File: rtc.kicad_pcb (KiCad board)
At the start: 2 copper layers, 50 x 30 mm, 8 parts, among them J1 Conn_01x05, U1 DS1302N+, Y1 32.768kHz

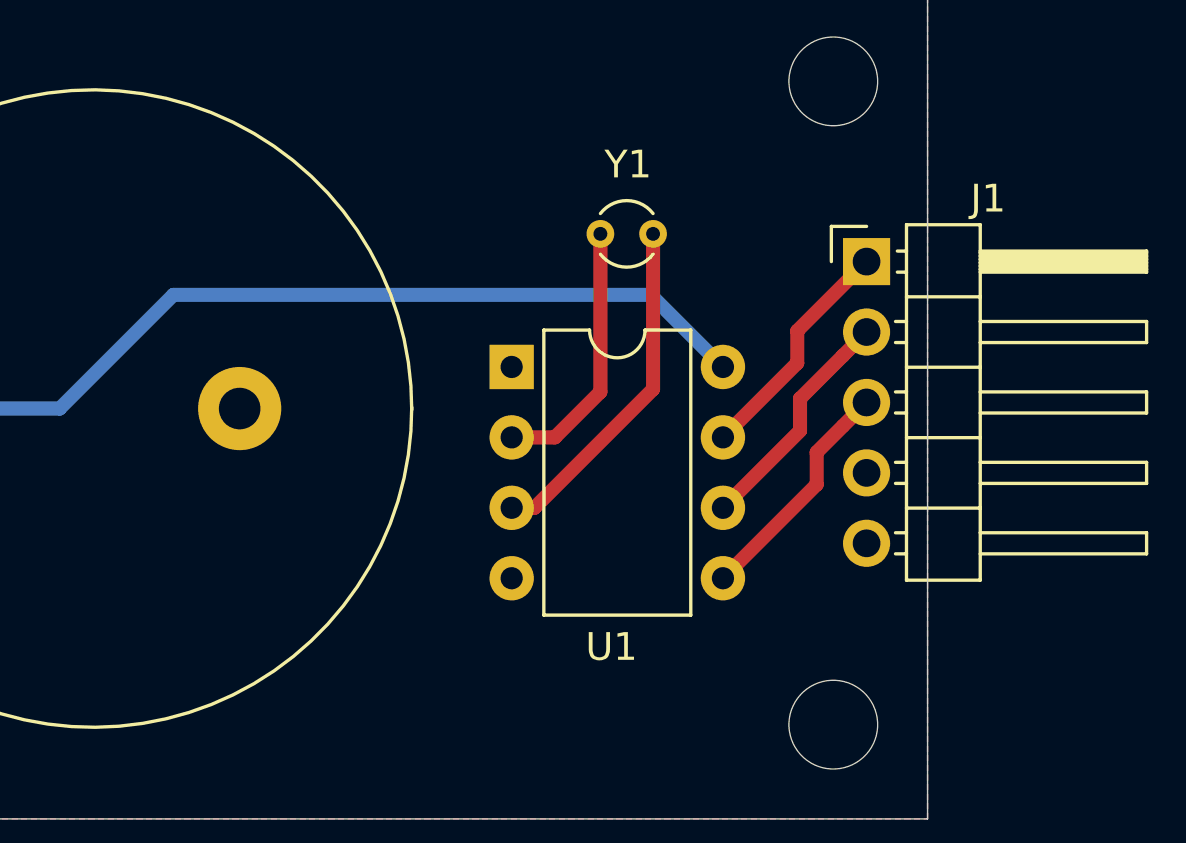
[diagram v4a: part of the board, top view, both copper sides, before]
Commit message: Clean up silk screen labels
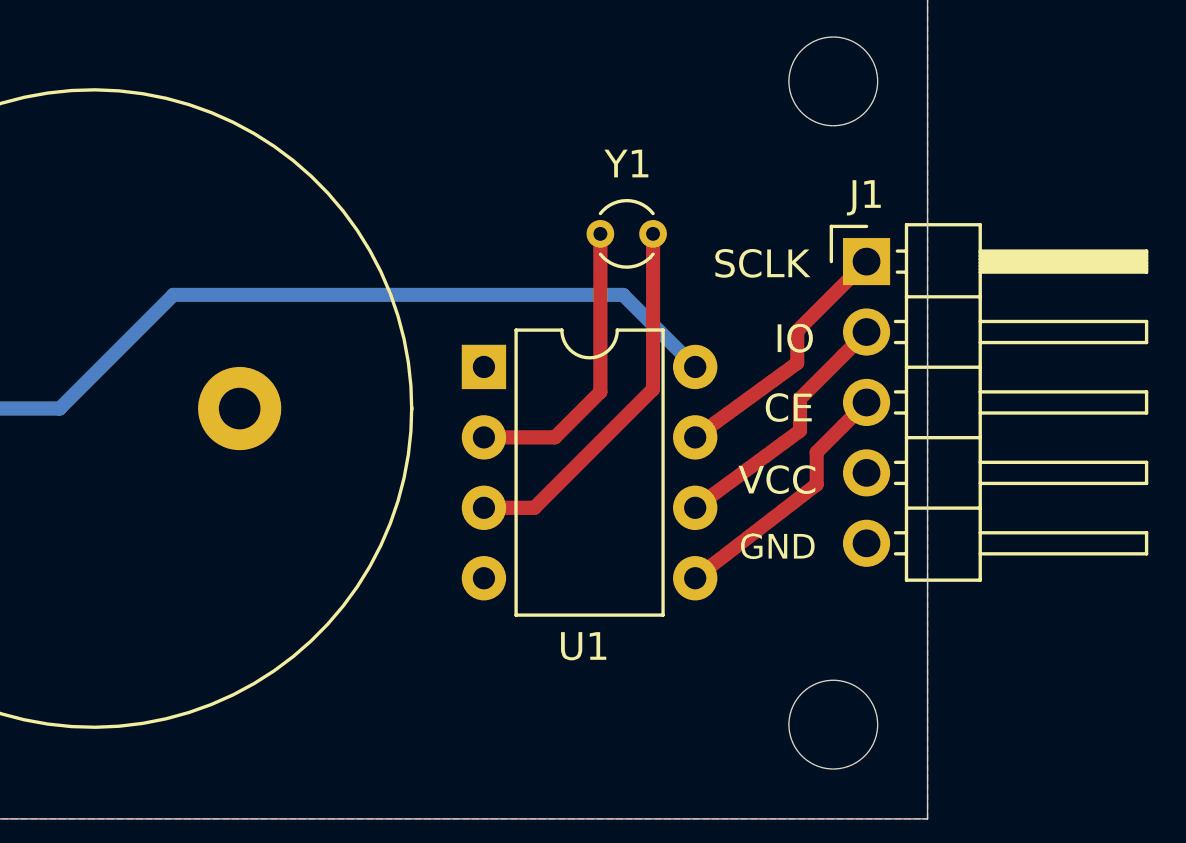
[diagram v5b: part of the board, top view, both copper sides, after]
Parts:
- moved U1 1.00 mm to (60.0, 44.7)
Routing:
- net Net-(U1-Pad3): track 12.5 -> 13.5 mm
- net Net-(U1-Pad2): track 9.58 -> 10.6 mm
- net Net-(BT1-Pad1): track 40.7 -> 39.7 mm
- net /SCLK: track 8.49 -> 9.25 mm
- net /IO: track 8.49 -> 9.25 mm
- net /CE: track 8.49 -> 9.24 mm
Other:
- board text added: "CE"
- board text added: "GND"
- board text added: "IO"
- board text added: "SCLK"
- board text added: "VCC"
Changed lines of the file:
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@@
   (general
     (thickness 1.6)
-    (drawings 15)
+    (drawings 20)
     (tracks 22)
     (zones 0)
@@
   )
   (module Package_DIP:DIP-8_W7.62mm (layer F.Cu)
-    (at 61 44.7)
+    (at 60 44.7)
     (descr "8-lead though-hole mounted DIP package, row spacing 7.62 mm (300 mils)")
     (tags "THT DIP DIL PDIP 2.54mm 7.62mm 300mil")
@@
     (descr "Through hole angled pin header, 1x05, 2.54mm pitch, 6mm pin length, single row")
     (tags "Through hole angled pin header THT 1x05 2.54mm single row")
-    (fp_text reference J1 (at 4.385 -2.27) (layer F.SilkS)
+    (fp_text reference J1 (at 0 -2.4) (layer F.SilkS)
       (effects (font (size 1 1) (thickness 0.15)))
     )
@@
     )
   )
+  (gr_text SCLK (at 70 41) (layer F.SilkS)
+    (effects (font (size 1 1) (thickness 0.15)))
+  )
+  (gr_text IO (at 71.2 43.7) (layer F.SilkS)
+    (effects (font (size 1 1) (thickness 0.15)))
+  )
+  (gr_text CE (at 71 46.2) (layer F.SilkS)
+    (effects (font (size 1 1) (thickness 0.15)))
+  )
+  (gr_text VCC (at 70.6 48.8) (layer F.SilkS)
+    (effects (font (size 1 1) (thickness 0.15)))
+  )
+  (gr_text GND (at 70.6 51.2) (layer F.SilkS)
+    (effects (font (size 0.889 0.889) (thickness 0.15)))
+  )
   (dimension 3.4 (width 0.12) (layer Dwgs.User)
     (gr_text "3.400 mm" (at 78.47 32.7 90) (layer Dwgs.User)
@@
   )
   (via (at 32.1 46) (size 0.762) (drill 0.4318) (layers F.Cu B.Cu) (net 2))
-  (segment (start 66.02 42.1) (end 68.62 44.7) (width 0.508) (layer B.Cu) (net 2))
-  (segment (start 48.8 42.1) (end 66.02 42.1) (width 0.508) (layer B.Cu) (net 2))
   (segment (start 30.7 46.2) (end 44.7 46.2) (width 0.508) (layer B.Cu) (net 2))
   (segment (start 44.7 46.2) (end 48.8 42.1) (width 0.508) (layer B.Cu) (net 2))
+  (segment (start 65.02 42.1) (end 67.62 44.7) (width 0.508) (layer B.Cu) (net 2))
+  (segment (start 48.8 42.1) (end 65.02 42.1) (width 0.508) (layer B.Cu) (net 2))
   (segment (start 71.3 43.4) (end 73.8 40.9) (width 0.508) (layer F.Cu) (net 4))
-  (segment (start 68.62 47.24) (end 71.3 44.56) (width 0.508) (layer F.Cu) (net 4))
+  (segment (start 67.62 47.24) (end 71.3 44.56) (width 0.508) (layer F.Cu) (net 4))
   (segment (start 71.3 44.56) (end 71.3 43.4) (width 0.508) (layer F.Cu) (net 4))
   (segment (start 72.950001 44.289999) (end 73.8 43.44) (width 0.508) (layer F.Cu) (net 5))
   (segment (start 71.4 45.84) (end 72.950001 44.289999) (width 0.508) (layer F.Cu) (net 5))
-  (segment (start 68.62 49.78) (end 71.4 47) (width 0.508) (layer F.Cu) (net 5))
+  (segment (start 67.62 49.78) (end 71.4 47) (width 0.508) (layer F.Cu) (net 5))
   (segment (start 71.4 47) (end 71.4 45.84) (width 0.508) (layer F.Cu) (net 5))
   (segment (start 72.950001 46.829999) (end 73.8 45.98) (width 0.508) (layer F.Cu) (net 6))
   (segment (start 72 47.78) (end 72.950001 46.829999) (width 0.508) (layer F.Cu) (net 6))
-  (segment (start 68.62 52.32) (end 72 48.94) (width 0.508) (layer F.Cu) (net 6))
+  (segment (start 67.62 52.32) (end 72 48.94) (width 0.508) (layer F.Cu) (net 6))
   (segment (start 72 48.94) (end 72 47.78) (width 0.508) (layer F.Cu) (net 6))
-  (segment (start 62.56 47.24) (end 61 47.24) (width 0.508) (layer F.Cu) (net 7))
+  (segment (start 62.56 47.24) (end 60 47.24) (width 0.508) (layer F.Cu) (net 7))
   (segment (start 64.2 39.9) (end 64.2 45.6) (width 0.508) (layer F.Cu) (net 7))
   (segment (start 64.2 45.6) (end 62.56 47.24) (width 0.508) (layer F.Cu) (net 7))
-  (segment (start 61.82 49.78) (end 61 49.78) (width 0.508) (layer F.Cu) (net 8))
+  (segment (start 61.82 49.78) (end 60 49.78) (width 0.508) (layer F.Cu) (net 8))
   (segment (start 66.1 39.9) (end 66.1 45.5) (width 0.508) (layer F.Cu) (net 8))
   (segment (start 66.1 45.5) (end 61.82 49.78) (width 0.508) (layer F.Cu) (net 8))

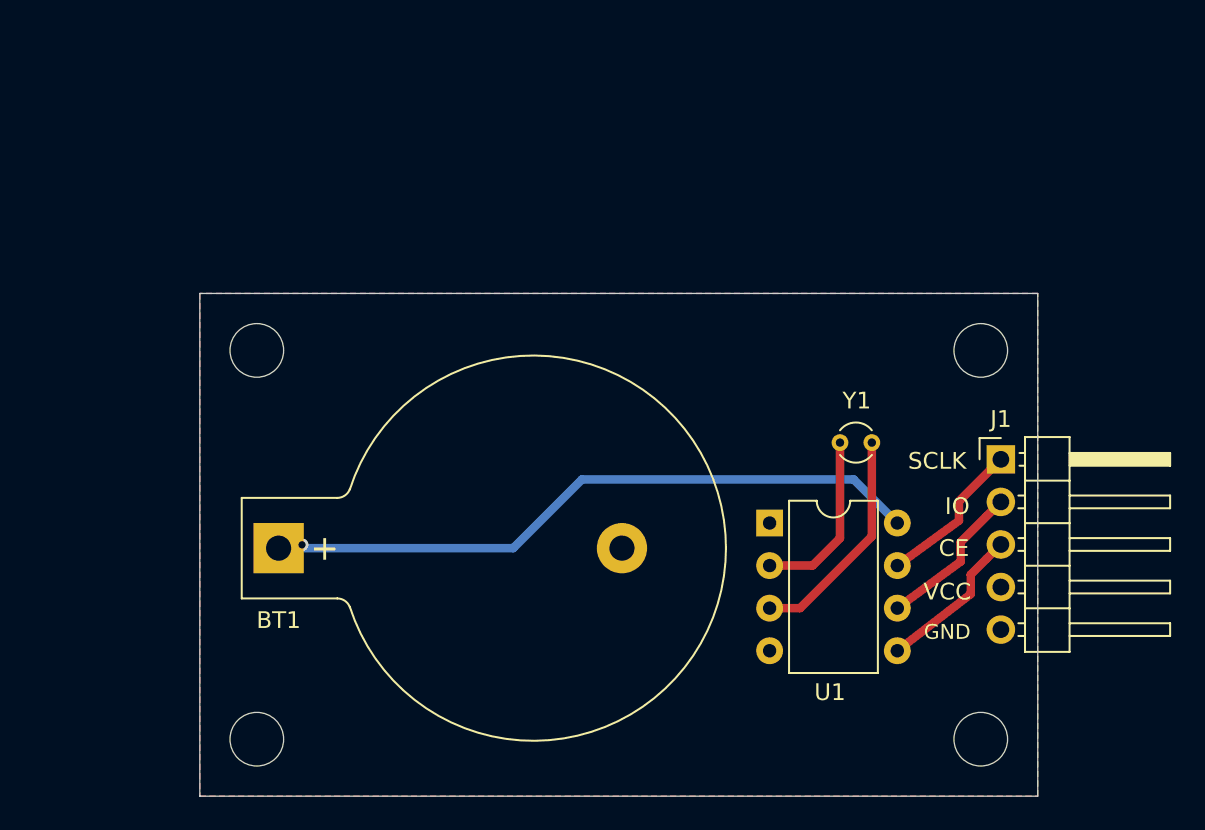
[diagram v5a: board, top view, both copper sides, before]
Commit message: Round edgecuts
- New project footprint library rtc.pretty
- Added logo to silkscreen
- Added title/rev to silkscreen
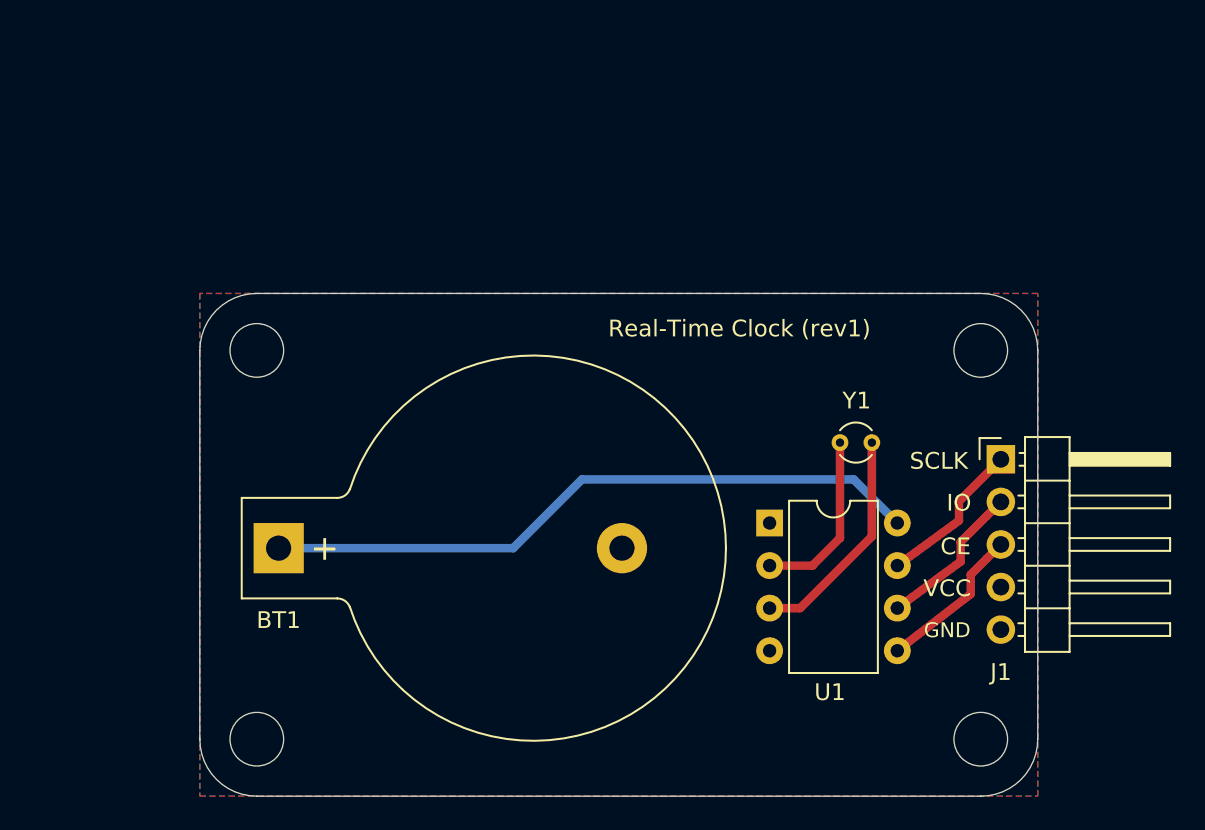
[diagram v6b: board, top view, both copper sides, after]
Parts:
- added G***: LOGO, rtc:tf, B.Cu at (51.1, 56.8)
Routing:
- net Net-(BT1-Pad1): vias 1 -> 0
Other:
- outline, holes or cut-outs redrawn
- board text added: "Real-Time Clock (rev1)"
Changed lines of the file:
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@@
   (general
     (thickness 1.6)
-    (drawings 20)
-    (tracks 22)
+    (drawings 25)
+    (tracks 21)
     (zones 0)
-    (modules 8)
+    (modules 9)
     (nets 9)
   )
@@
     (add_net "Net-(U1-Pad3)")
   )
+  (module rtc:tf (layer B.Cu)
+    (at 51.1 56.8 180)
+    (fp_text reference G*** (at 0 3.302) (layer B.SilkS) hide
+      (effects (font (size 1.524 1.524) (thickness 0.3)) (justify mirror))
+    )
+    (fp_text value LOGO (at 0.254 -4.318) (layer B.SilkS) hide
+      (effects (font (size 1.524 1.524) (thickness 0.3)) (justify mirror))
+    )
+    (fp_poly (pts (xy 9.397542 -0.342483) (xy 9.70121 -0.425407) (xy 9.508103 -0.476614) (xy 9.132338 -0.498327)
+      (xy 8.432829 -0.635382) (xy 8.113939 -1.016561) (xy 8.098522 -1.069474) (xy 7.861888 -1.528523)
+      (xy 7.608517 -1.536367) (xy 7.486407 -1.091776) (xy 7.486316 -1.074568) (xy 7.721193 -0.60563)
+      (xy 8.336455 -0.333978) (xy 9.198053 -0.310959) (xy 9.397542 -0.342483)) (layer B.SilkS) (width 0.01))
+    (fp_poly (pts (xy 5.036959 1.203157) (xy 4.988488 0.394975) (xy 4.853621 -0.538575) (xy 4.82797 -0.668422)
+      (xy 4.689355 -1.285494) (xy 4.616497 -1.408256) (xy 4.580968 -1.068772) (xy 4.57601 -0.95261)
+      (xy 4.545263 -0.167324) (xy 3.752825 -0.926528) (xy 3.196747 -1.394404) (xy 2.824799 -1.497459)
+      (xy 2.566758 -1.35905) (xy 2.066945 -1.171946) (xy 1.638879 -1.318289) (xy 1.137363 -1.560244)
+      (xy 0.875056 -1.559039) (xy 0.712983 -1.425965) (xy 0.569985 -1.038711) (xy 0.542867 -0.690702)
+      (xy 0.574598 -0.305412) (xy 0.717262 -0.425345) (xy 0.834449 -0.621106) (xy 1.07072 -0.947759)
+      (xy 1.323709 -0.902849) (xy 1.652572 -0.624655) (xy 2.061943 -0.301031) (xy 2.318463 -0.35167)
+      (xy 2.550137 -0.637069) (xy 2.815408 -0.93761) (xy 3.085826 -0.942668) (xy 3.541076 -0.630914)
+      (xy 3.706253 -0.499835) (xy 4.323889 0.193421) (xy 4.74617 1.016115) (xy 4.762105 1.069473)
+      (xy 5.024734 2.005262) (xy 5.036959 1.203157)) (layer B.SilkS) (width 0.01))
+    (fp_poly (pts (xy -7.040702 -1.425965) (xy -7.077403 -1.584916) (xy -7.218947 -1.604211) (xy -7.439022 -1.506385)
+      (xy -7.397193 -1.425965) (xy -7.079889 -1.393967) (xy -7.040702 -1.425965)) (layer B.SilkS) (width 0.01))
+    (fp_poly (pts (xy -8.079364 1.257407) (xy -8.149744 0.824839) (xy -8.202011 0.234202) (xy -7.967407 -0.038959)
+      (xy -7.836777 -0.08261) (xy -7.541688 -0.198289) (xy -7.721347 -0.324736) (xy -7.95421 -0.403896)
+      (xy -8.421605 -0.685812) (xy -8.555789 -0.951194) (xy -8.732233 -1.393125) (xy -8.823158 -1.470527)
+      (xy -9.046503 -1.403277) (xy -9.090526 -1.181571) (xy -9.288307 -0.661128) (xy -9.558421 -0.37219)
+      (xy -9.864127 -0.10091) (xy -9.695054 -0.01656) (xy -9.450892 -0.008504) (xy -8.914577 0.225052)
+      (xy -8.595853 0.802105) (xy -8.319827 1.421569) (xy -8.126968 1.574391) (xy -8.079364 1.257407)) (layer B.SilkS) (width 0.01))
+    (fp_poly (pts (xy 6.936383 -0.391661) (xy 7.213177 -0.732866) (xy 7.021993 -1.002148) (xy 6.651473 -1.069474)
+      (xy 6.265228 -1.128012) (xy 6.342801 -1.377563) (xy 6.416842 -1.470527) (xy 6.582542 -1.794378)
+      (xy 6.353486 -1.831571) (xy 5.815263 -1.582795) (xy 5.426822 -1.186554) (xy 5.347369 -0.927598)
+      (xy 5.554907 -0.62386) (xy 6.238597 -0.62386) (xy 6.275298 -0.78281) (xy 6.416842 -0.802106)
+      (xy 6.636917 -0.70428) (xy 6.595088 -0.62386) (xy 6.277784 -0.591861) (xy 6.238597 -0.62386)
+      (xy 5.554907 -0.62386) (xy 5.574535 -0.595135) (xy 6.095812 -0.361382) (xy 6.670864 -0.307398)
+      (xy 6.936383 -0.391661)) (layer B.SilkS) (width 0.01))
+    (fp_poly (pts (xy 0.069953 -0.25455) (xy 0.267369 -0.784307) (xy 0.039108 -1.377596) (xy -0.530172 -1.736982)
+      (xy -1.267226 -1.775089) (xy -1.537368 -1.694506) (xy -1.847488 -1.345958) (xy -1.817606 -1.002632)
+      (xy -1.53903 -1.002632) (xy -1.438886 -1.275056) (xy -0.977798 -1.320725) (xy -0.42292 -1.174553)
+      (xy -0.055513 -0.9037) (xy 0 -0.755741) (xy -0.208263 -0.583829) (xy -0.682095 -0.585056)
+      (xy -1.195059 -0.723096) (xy -1.52072 -0.961625) (xy -1.53903 -1.002632) (xy -1.817606 -1.002632)
+      (xy -1.803162 -0.836682) (xy -1.447039 -0.364086) (xy -1.220208 -0.226489) (xy -0.46295 -0.050827)
+      (xy 0.069953 -0.25455)) (layer B.SilkS) (width 0.01))
+    (fp_poly (pts (xy -2.33438 1.285024) (xy -1.719044 1.109998) (xy -1.391317 0.803622) (xy -1.390854 0.802105)
+      (xy -1.361722 0.546861) (xy -1.607245 0.719277) (xy -1.624263 0.735263) (xy -2.276246 1.050402)
+      (xy -2.938849 0.867841) (xy -3.326944 0.475245) (xy -3.680514 -0.12701) (xy -3.632131 -0.437713)
+      (xy -3.15362 -0.547719) (xy -3.007895 -0.553529) (xy -2.544847 -0.588254) (xy -2.575639 -0.682488)
+      (xy -2.78742 -0.774004) (xy -3.287775 -1.136963) (xy -3.455841 -1.403747) (xy -3.618513 -1.683461)
+      (xy -3.898496 -1.599561) (xy -4.14421 -1.419959) (xy -4.473177 -1.06666) (xy -4.344737 -0.882828)
+      (xy -4.053546 -0.54233) (xy -4.010526 -0.304579) (xy -3.783172 0.512089) (xy -3.2003 1.090811)
+      (xy -2.410692 1.290486) (xy -2.33438 1.285024)) (layer B.SilkS) (width 0.01))
+  )
   (module MountingHole:MountingHole_3.2mm_M3_ISO7380 locked (layer F.Cu)
     (at 29.4 34.4)
@@
     (descr "Through hole angled pin header, 1x05, 2.54mm pitch, 6mm pin length, single row")
     (tags "Through hole angled pin header THT 1x05 2.54mm single row")
-    (fp_text reference J1 (at 0 -2.4) (layer F.SilkS)
+    (fp_text reference J1 (at 0 12.7) (layer F.SilkS)
       (effects (font (size 1 1) (thickness 0.15)))
     )
@@
     )
   )
-  (gr_text SCLK (at 70 41) (layer F.SilkS)
+  (gr_arc (start 72.6 34.4) (end 76 34.4) (angle -90) (layer Edge.Cuts) (width 0.05))
+  (gr_arc (start 72.6 57.6) (end 72.6 61) (angle -90) (layer Edge.Cuts) (width 0.05))
+  (gr_arc (start 29.4 57.6) (end 26 57.6) (angle -90) (layer Edge.Cuts) (width 0.05))
+  (gr_arc (start 29.4 34.4) (end 29.4 31) (angle -90) (layer Edge.Cuts) (width 0.05))
+  (gr_text "Real-Time Clock (rev1)" (at 58.2 33.1) (layer F.SilkS)
     (effects (font (size 1 1) (thickness 0.15)))
   )
-  (gr_text IO (at 71.2 43.7) (layer F.SilkS)
+  (gr_text SCLK (at 70.1 41) (layer F.SilkS)
     (effects (font (size 1 1) (thickness 0.15)))
   )
-  (gr_text CE (at 71 46.2) (layer F.SilkS)
+  (gr_text IO (at 71.3 43.5) (layer F.SilkS)
     (effects (font (size 1 1) (thickness 0.15)))
   )
-  (gr_text VCC (at 70.6 48.8) (layer F.SilkS)
+  (gr_text CE (at 71.1 46.1) (layer F.SilkS)
     (effects (font (size 1 1) (thickness 0.15)))
   )
-  (gr_text GND (at 70.6 51.2) (layer F.SilkS)
+  (gr_text VCC (at 70.6 48.6) (layer F.SilkS)
+    (effects (font (size 1 1) (thickness 0.15)))
+  )
+  (gr_text GND (at 70.6 51.1) (layer F.SilkS)
     (effects (font (size 0.889 0.889) (thickness 0.15)))
   )
@@
     (arrow2b (pts (xy 78.25 61) (xy 77.663579 59.873496)))
   )
-  (gr_line (start 76 31) (end 26 31) (layer Edge.Cuts) (width 0.05))
-  (gr_line (start 76 61) (end 76 31) (layer Edge.Cuts) (width 0.05))
-  (gr_line (start 26 61) (end 76 61) (layer Edge.Cuts) (width 0.05))
-  (gr_line (start 26 31) (end 26 61) (layer Edge.Cuts) (width 0.05))
+  (gr_line (start 72.6 31) (end 29.4 31) (layer Edge.Cuts) (width 0.05))
+  (gr_line (start 76 57.6) (end 76 34.4) (layer Edge.Cuts) (width 0.05))
+  (gr_line (start 29.4 61) (end 72.6 61) (layer Edge.Cuts) (width 0.05))
+  (gr_line (start 26 34.4) (end 26 57.6) (layer Edge.Cuts) (width 0.05))
   (dimension 50 (width 0.15) (layer Dwgs.User)
     (gr_text "50.000 mm" (at 51 19.7) (layer Dwgs.User)
@@
     (arrow2b (pts (xy 18 31) (xy 18.586421 32.126504)))
   )
-  (via (at 32.1 46) (size 0.762) (drill 0.4318) (layers F.Cu B.Cu) (net 2))
+  (segment (start 44.7 46.2) (end 48.8 42.1) (width 0.508) (layer B.Cu) (net 2))
   (segment (start 30.7 46.2) (end 44.7 46.2) (width 0.508) (layer B.Cu) (net 2))
-  (segment (start 44.7 46.2) (end 48.8 42.1) (width 0.508) (layer B.Cu) (net 2))
+  (segment (start 48.8 42.1) (end 65.02 42.1) (width 0.508) (layer B.Cu) (net 2))
   (segment (start 65.02 42.1) (end 67.62 44.7) (width 0.508) (layer B.Cu) (net 2))
-  (segment (start 48.8 42.1) (end 65.02 42.1) (width 0.508) (layer B.Cu) (net 2))
   (segment (start 71.3 43.4) (end 73.8 40.9) (width 0.508) (layer F.Cu) (net 4))
   (segment (start 67.62 47.24) (end 71.3 44.56) (width 0.508) (layer F.Cu) (net 4))
